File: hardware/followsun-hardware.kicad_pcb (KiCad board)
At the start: 2 copper layers, 75.4 x 66 mm, 41 parts, among them J1 PowerSupply, J2 5V StepDown, J3 AzimuthSense, J4 ElevationSense, J5 Wind, J6 DS3231_Module, J7 AzimuthMotor, J8 ElevationMotor, K1 SANYOU_SRD_Form_C, K2 SANYOU_SRD_Form_C, K3 SANYOU_SRD_Form_C, K4 SANYOU_SRD_Form_C, SW1 WindMode, U1 LM4040DBZ-4.1, U2 ULN2803A

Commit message: v1.0
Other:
- outline, holes or cut-outs redrawn
- board text added: "Version 1.0 | 2019-11-11"
- board text removed: "Version 1.0"
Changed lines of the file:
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@@
   (general
     (thickness 1.6)
-    (drawings 26)
+    (drawings 34)
     (tracks 270)
     (zones 0)
@@
   (layers
     (0 F.Cu signal)
-    (31 B.Cu signal hide)
-    (32 B.Adhes user)
+    (31 B.Cu signal)
+    (32 B.Adhes user hide)
     (33 F.Adhes user)
-    (34 B.Paste user)
-    (35 F.Paste user)
-    (36 B.SilkS user)
-    (37 F.SilkS user)
-    (38 B.Mask user)
-    (39 F.Mask user)
-    (40 Dwgs.User user)
-    (41 Cmts.User user)
-    (42 Eco1.User user)
-    (43 Eco2.User user)
+    (34 B.Paste user hide)
+    (35 F.Paste user hide)
+    (36 B.SilkS user hide)
+    (37 F.SilkS user hide)
+    (38 B.Mask user hide)
+    (39 F.Mask user hide)
+    (40 Dwgs.User user hide)
+    (41 Cmts.User user hide)
+    (42 Eco1.User user hide)
+    (43 Eco2.User user hide)
     (44 Edge.Cuts user)
-    (45 Margin user)
-    (46 B.CrtYd user)
-    (47 F.CrtYd user)
-    (48 B.Fab user)
-    (49 F.Fab user)
+    (45 Margin user hide)
+    (46 B.CrtYd user hide)
+    (47 F.CrtYd user hide)
+    (48 B.Fab user hide)
+    (49 F.Fab user hide)
   )
   (setup
@@
       (layerselection 0x010fc_ffffffff)
       (usegerberextensions false)
-      (usegerberattributes false)
+      (usegerberattributes true)
       (usegerberadvancedattributes false)
       (creategerberjobfile false)
@@
       (plotinvisibletext false)
       (padsonsilk false)
-      (subtractmaskfromsilk false)
+      (subtractmaskfromsilk true)
       (outputformat 1)
       (mirror false)
-      (drillshape 1)
+      (drillshape 0)
       (scaleselection 1)
-      (outputdirectory ""))
+      (outputdirectory "output/v1.0/"))
   )
   (net 0 "")
@@
     )
   )
-  (gr_text "Version 1.0" (at 154.2542 96.774) (layer F.SilkS)
+  (gr_arc (start 206.0575 68.3895) (end 207.0735 68.3895) (angle -180.0000564) (layer Edge.Cuts) (width 0.05))
+  (gr_line (start 205.0415 72.3265) (end 205.0415 68.389501) (layer Edge.Cuts) (width 0.05))
+  (gr_line (start 207.0735 68.3895) (end 207.0735 72.326499) (layer Edge.Cuts) (width 0.05))
+  (gr_arc (start 206.0575 72.3265) (end 205.0415 72.3265) (angle -180.0000564) (layer Edge.Cuts) (width 0.05))
+  (gr_line (start 207.0735 77.724) (end 207.0735 81.660999) (layer Edge.Cuts) (width 0.05))
+  (gr_line (start 205.0415 81.661) (end 205.0415 77.724001) (layer Edge.Cuts) (width 0.05))
+  (gr_arc (start 206.0575 81.661) (end 205.0415 81.661) (angle -180.0000564) (layer Edge.Cuts) (width 0.05))
+  (gr_arc (start 206.0575 77.724) (end 207.0735 77.724) (angle -180.0000564) (layer Edge.Cuts) (width 0.05))
+  (gr_text "Version 1.0 | 2019-11-11" (at 159.3215 96.8375) (layer F.SilkS)
     (effects (font (size 0.8 0.8) (thickness 0.1)))
   )

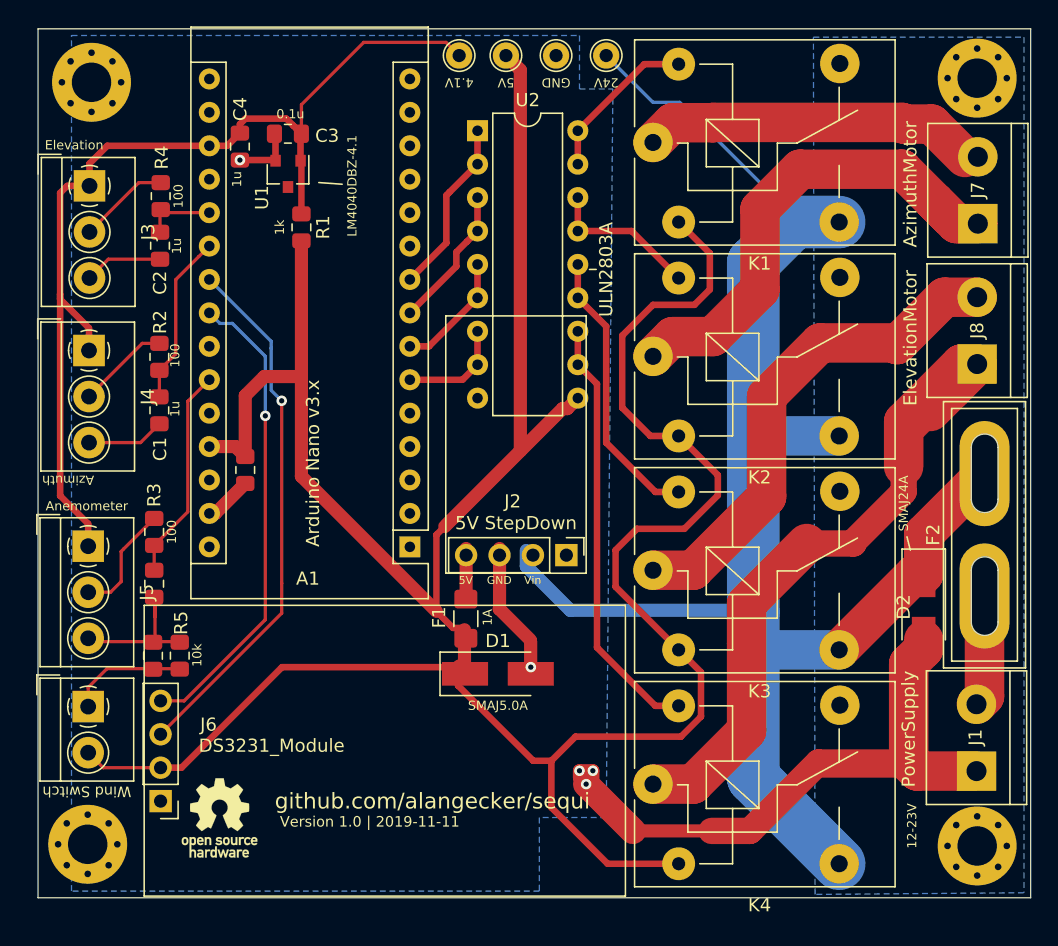
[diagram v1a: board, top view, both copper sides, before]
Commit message: major update with L298, sd cards, LEDs
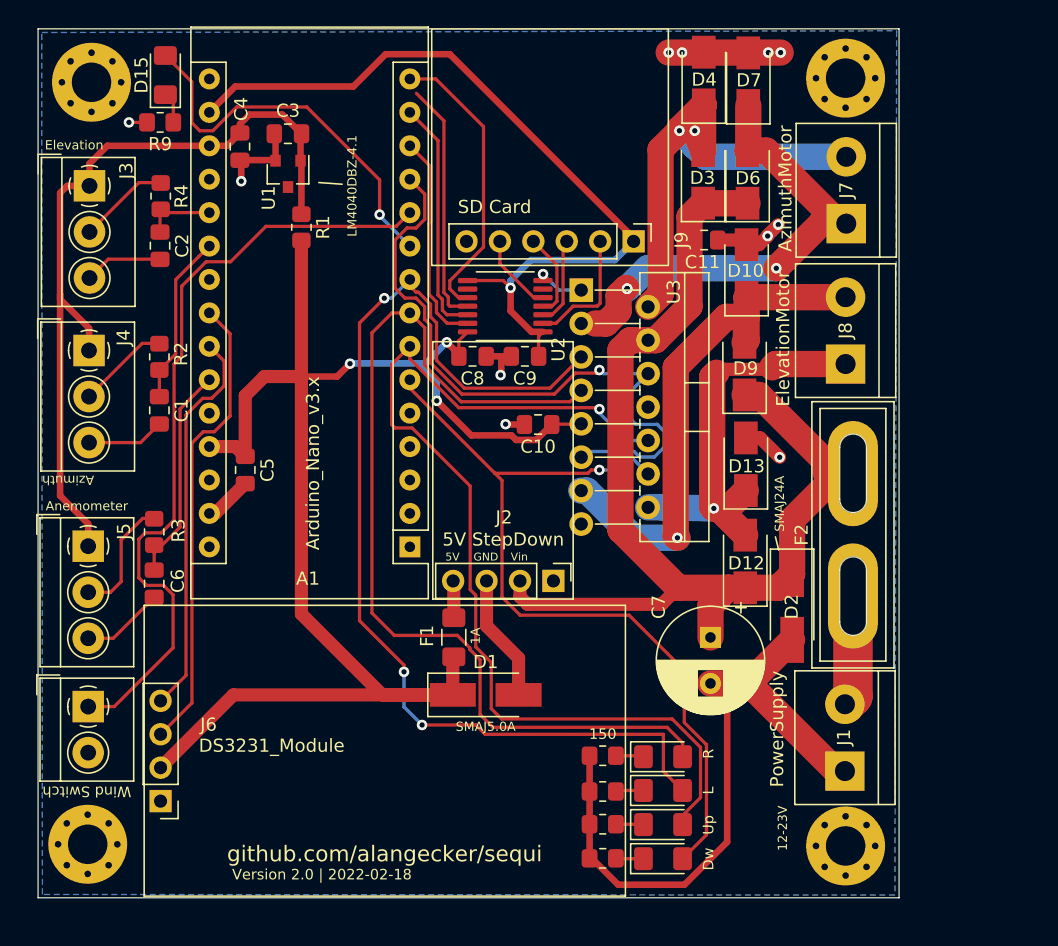
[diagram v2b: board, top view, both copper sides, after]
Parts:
- removed K1, K2, K3, K4: SANYOU_SRD_Form_C, Relay_THT:Relay_SPDT_SANYOU_SRD_Series_Form_C
- removed REF**: OSHW-Logo_5.7x6mm_SilkScreen, Symbol:OSHW-Logo_5.7x6mm_SilkScreen
- removed TP3: 24V, TestPoint:TestPoint_THTPad_D2.0mm_Drill1.0mm
- removed TP4: 5V, TestPoint:TestPoint_THTPad_D2.0mm_Drill1.0mm
- removed TP5: GND, TestPoint:TestPoint_THTPad_D2.0mm_Drill1.0mm
- removed TP6: 4.1V, TestPoint:TestPoint_THTPad_D2.0mm_Drill1.0mm
- added C10: 100n, Capacitor_SMD:C_0805_2012Metric_Pad1.18x1.45mm_HandSolder, F.Cu at (172.1, 66.6)
- added C11: 100n, Capacitor_SMD:C_0805_2012Metric_Pad1.18x1.45mm_HandSolder, F.Cu at (184.7, 52.6)
- added C8: 100n, Capacitor_SMD:C_0805_2012Metric_Pad1.18x1.45mm_HandSolder, F.Cu at (167.1, 61.5)
- added C9: 100n, Capacitor_SMD:C_0805_2012Metric_Pad1.18x1.45mm_HandSolder, F.Cu at (171.1, 61.5)
- added D10: US1G, Diode_SMD:D_SMA, F.Cu at (188.0, 55.0)
- added D11: LED, LED_SMD:LED_1206_3216Metric_Pad1.42x1.75mm_HandSolder, F.Cu at (181.6, 91.9)
- added D12: US1G, Diode_SMD:D_SMA, F.Cu at (187.9, 77.1)
- added D13: US1G, Diode_SMD:D_SMA, F.Cu at (187.9, 69.7)
- added D14: LED, LED_SMD:LED_1206_3216Metric_Pad1.42x1.75mm_HandSolder, F.Cu at (181.6, 94.5)
- added D15: LED, LED_SMD:LED_1206_3216Metric_Pad1.42x1.75mm_HandSolder, F.Cu at (143.8, 40.1)
- added D3: US1G, Diode_SMD:D_SMA, F.Cu at (184.7, 47.8)
- added D4: US1G, Diode_SMD:D_SMA, F.Cu at (184.7, 40.4)
- added D5: LED, LED_SMD:LED_1206_3216Metric_Pad1.42x1.75mm_HandSolder, F.Cu at (181.6, 99.6)
- added D6: US1G, Diode_SMD:D_SMA, F.Cu at (188.0, 47.8)
- added D7: US1G, Diode_SMD:D_SMA, F.Cu at (188.1, 40.4)
- added D8: LED, LED_SMD:LED_1206_3216Metric_Pad1.42x1.75mm_HandSolder, F.Cu at (181.6, 97.1)
- added D9: US1G, Diode_SMD:D_SMA, F.Cu at (187.8, 62.4)
- added J9: 3.3V SD Module, Connector_PinHeader_2.54mm:PinHeader_1x06_P2.54mm_Vertical, F.Cu at (179.4, 52.7)
- added R6: 150, Resistor_SMD:R_0805_2012Metric_Pad1.20x1.40mm_HandSolder, F.Cu at (177.0, 97.0)
- added R7: 150, Resistor_SMD:R_0805_2012Metric_Pad1.20x1.40mm_HandSolder, F.Cu at (177.0, 91.8)
- added R8: 150, Resistor_SMD:R_0805_2012Metric_Pad1.20x1.40mm_HandSolder, F.Cu at (177.0, 94.5)
- added R9: 150, Resistor_SMD:R_0805_2012Metric_Pad1.20x1.40mm_HandSolder, F.Cu at (143.4, 43.7)
- added U3: L298HN, Package_TO_SOT_THT:TO-220-15_P2.54x2.54mm_StaggerOdd_Lead4.58mm_Vertical, F.Cu at (175.4, 56.4)
- A1: value Arduino Nano v3.x -> Arduino_Nano_v3.x
- C1, C2, C3, C4, C5, C6: footprint Capacitor_SMD:C_0805_2012Metric_Pad1.15x1.40mm_HandSolder -> Capacitor_SMD:C_0805_2012Metric_Pad1.18x1.45mm_HandSolder
- C7: value Reserved -> 100u 50V; footprint Capacitor_SMD:C_0805_2012Metric_Pad1.15x1.40mm_HandSolder -> Capacitor_THT:CP_Radial_D8.0mm_P3.50mm
- R1, R2, R3, R4: footprint Resistor_SMD:R_0805_2012Metric_Pad1.15x1.40mm_HandSolder -> Resistor_SMD:R_0805_2012Metric_Pad1.20x1.40mm_HandSolder
- R5: value 10k -> 150; footprint Resistor_SMD:R_0805_2012Metric_Pad1.15x1.40mm_HandSolder -> Resistor_SMD:R_0805_2012Metric_Pad1.20x1.40mm_HandSolder
- U2: value ULN2803A -> TXB0104PW; footprint Package_DIP:DIP-18_W7.62mm -> Package_SO:TSSOP-14_4.4x5mm_P0.65mm
- moved C7 42.4 mm to (185.2, 82.8), turned to -90 degrees
- moved R5 35.6 mm to (177.0, 99.6), turned to 180 degrees
- moved U2 13.5 mm to (169.6, 57.7), turned to 180 degrees
- moved D2 10.0 mm to (191.4, 80.5)
- moved F2 10.0 mm to (196.0, 79.7)
- moved H2 10.0 mm to (195.5, 40.3)
- moved H4 10.0 mm to (195.5, 98.7)
- moved J1 10.0 mm to (195.4, 93.0)
- moved J7 10.0 mm to (195.5, 51.4)
- moved J8 10.0 mm to (195.5, 62.1)
- moved J2 2.19 mm to (164.1, 79.9)
- moved D1 1.85 mm to (168.1, 87.2)
- moved F1 1.68 mm to (165.7, 82.8)
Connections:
- A1 pad 1: Net-(A1-Pad1) -> unconnected-(A1-Pad1)
- A1 pad 10: Net-(A1-Pad10) -> /Status_LED
- A1 pad 12: Net-(A1-Pad12) -> /MOTOR_EN
- A1 pad 13: Net-(A1-Pad13) -> /SS
- A1 pad 14: Net-(A1-Pad14) -> /MOSI
- A1 pad 15: Net-(A1-Pad15) -> /MISO
- A1 pad 16: Net-(A1-Pad16) -> /SCK
- A1 pad 17: Net-(A1-Pad17) -> +3V3
- A1 pad 19: Net-(A1-Pad19) -> unconnected-(A1-Pad19)
- A1 pad 2: Net-(A1-Pad2) -> unconnected-(A1-Pad2)
- A1 pad 22: /SDA -> unconnected-(A1-Pad22)
- A1 pad 23: /SCL -> /SDA
- A1 pad 24: Net-(A1-Pad24) -> /SCL
- A1 pad 26: Net-(A1-Pad26) -> unconnected-(A1-Pad26)
- A1 pad 28: Net-(A1-Pad28) -> unconnected-(A1-Pad28)
- A1 pad 3: Net-(A1-Pad3) -> unconnected-(A1-Pad3)
- A1 pad 30: Net-(A1-Pad30) -> unconnected-(A1-Pad30)
- A1 pad 5: Net-(A1-Pad5) -> unconnected-(A1-Pad5)
- C7 pad 1: /WindMode -> +24V
- J2 pad 1: Net-(J2-Pad1) -> unconnected-(J2-Pad1)
- R5 pad 1: /WindMode -> Net-(D5-Pad1)
- SW1 pad 1: /WindMode -> Net-(A1-Pad11)
- SW1 pad 2: +5V -> GND
- U2 pad 1: /Az_Left -> +3V3
- U2 pad 10: +5V -> /MISO
- U2 pad 11: Net-(K4-Pad5) -> /SCK
- U2 pad 12: Net-(K4-Pad5) -> /MOSI
- U2 pad 13: Net-(K3-Pad5) -> /SS
- U2 pad 14: Net-(K3-Pad5) -> +5V
- U2 pad 2: /Az_Left -> Net-(J9-Pad2)
- U2 pad 3: /Az_Right -> Net-(J9-Pad3)
- U2 pad 4: /Az_Right -> Net-(J9-Pad4)
- U2 pad 5: /Elevation_Up -> Net-(J9-Pad5)
- U2 pad 6: /Elevation_Up -> unconnected-(U2-Pad6)
- U2 pad 7: /Elevation_Down -> GND
- U2 pad 8: /Elevation_Down -> +3V3
- U2 pad 9: GND -> unconnected-(U2-Pad9)
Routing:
- net +5V: track 236.4 -> 112.3 mm, vias 0 -> 3
- net /Az_Left: track 13.4 -> 81.6 mm, vias 0 -> 3
- net /Elevation_Up: track 9.21 -> 77.4 mm, vias 0 -> 1
- net /Az_Right: track 10.9 -> 73.9 mm
- net +3V3: track 0.00 -> 61.6 mm, vias 0 -> 1
- net Net-(A1-Pad11): track 0.00 -> 59.3 mm
- net /Elevation_Down: track 8.16 -> 63.9 mm, vias 0 -> 1
- net /MOTOR_EN: track 0.00 -> 50.8 mm, vias 0 -> 1
- net +24V: track 131.5 -> 82.4 mm
- net Net-(K4-Pad5): track 32.7 -> 0.00 mm
- net /Status_LED: track 0.00 -> 29.5 mm, vias 0 -> 1
- net Net-(D12-Pad2): track 59.1 -> 31.8 mm, vias 0 -> 1
- net /MISO: track 0.00 -> 22.1 mm
- net Net-(K3-Pad5): track 21.5 -> 0.00 mm
- net /SCK: track 0.00 -> 18.6 mm
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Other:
- board size 75.4 x 66 mm -> 65.4 x 66 mm
- net class Default removed
- board text added: "Dw"
- board text added: "L"
- board text added: "R"
- board text added: "SD Card"
- board text added: "Up"
- board text added: "Version 2.0 | 2022-02-18"
- board text removed: "Version 1.0 | 2019-11-11"
